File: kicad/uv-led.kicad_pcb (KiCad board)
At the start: 2 copper layers, 100 x 8 mm, 10 parts, among them J1 JST_PH_B2B-PH-K_1x02_P2.00mm_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

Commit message: updated physical stackup and removed back paste
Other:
- board text added: "Manufacturing Instruction: - Material Aluminum - Finished thickness: 1.6 mm ± 0.16 mm - PCBs must be RoHS compliant - Do not edit artwork, e.g. to add logos or order numbers - Clean to meet IPC J-STD-001E, Class 2 after assembly"
- board text removed: "Manufacturing Instruction: - Material Aluminum - Finished thickness: 1.57 mm ± 0.13 mm - PCBs must be RoHS compliant - Do not edit artwork, e.g. to add logos or order numbers - Clean to meet IPC J-STD-001E, Class 2 after assembly"

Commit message: Fixed BOM (#18)
- Fixed JST PN
- Fixed LED temperature
- Bumped to v1.1.1
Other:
- board text added: "UV-LED Design: T. Guentzel Date: 2026-09 Version: 1.1.1"
- board text removed: "UV-LED Design: T. Guentzel Date: 2026-09 Version: 1.1.0"
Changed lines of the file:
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@@
 		(title "QUIPS-C UV-LED")
 		(date "2026-09-02")
-		(rev "1.1.0")
+		(rev "1.1.1")
 		(company "TU Darmstadt")
 		(comment 1 "Copyright (©) 2026, Tom Güntzel <tom.guentzel@physik.tu-darmstadt.de>")
@@
 		(capping no)
 		(filling no)
-		(zone_defaults)
 		(pcbplotparams
 			(layerselection 0x00000000_00000000_55555555_5755f5ff)
@@
 		(sheetname "/")
 		(sheetfile "uv-led.kicad_sch")
+		(units
+			(unit
+				(name "A")
+				(pins)
+			)
+		)
 		(attr exclude_from_bom)
 		(duplicate_pad_numbers_are_jumpers no)
@@
 				(font
 					(size 1.27 1.27)
-				)
-			)
-		)
-		(property "KiLib_Generator" "mounting_hardware/mounting_hole"
-			(at 0 0 0)
-			(layer "F.SilkS")
-			(hide yes)
-			(effects
-				(font
-					(size 1 1)
-					(thickness 0.15)
 				)
 			)
@@
 			)
 		)
-		(property "MN" ""
-			(at 0 0 0)
-			(unlocked yes)
-			(layer "F.Fab")
-			(hide yes)
-			(effects
-				(font
-					(size 1 1)
-					(thickness 0.15)
-				)
-			)
-		)
-		(property "Mfr" ""
-			(at 0 0 0)
-			(unlocked yes)
-			(layer "F.Fab")
-			(hide yes)
-			(effects
-				(font
-					(size 1 1)
-					(thickness 0.15)
-				)
-			)
-		)
-		(property "Temperature" "Top = 0 °C to 100 °C"
+		(property "Temperature" "Top = -40 °C to 95 °C"
 			(at 0 0 0)
 			(unlocked yes)
@@
 			)
 		)
-		(property "MN" ""
-			(at 0 0 0)
-			(unlocked yes)
-			(layer "F.Fab")
-			(hide yes)
-			(effects
-				(font
-					(size 1 1)
-					(thickness 0.15)
-				)
-			)
-		)
-		(property "Mfr" ""
-			(at 0 0 0)
-			(unlocked yes)
-			(layer "F.Fab")
-			(hide yes)
-			(effects
-				(font
-					(size 1 1)
-					(thickness 0.15)
-				)
-			)
-		)
-		(property "Temperature" "Top = 0 °C to 100 °C"
+		(property "Temperature" "Top = -40 °C to 95 °C"
 			(at 0 0 0)
 			(unlocked yes)
@@
 			)
 		)
-		(property "MN" ""
-			(at 0 0 0)
-			(unlocked yes)
-			(layer "F.Fab")
-			(hide yes)
-			(effects
-				(font
-					(size 1 1)
-					(thickness 0.15)
-				)
-			)
-		)
-		(property "Mfr" ""
-			(at 0 0 0)
-			(unlocked yes)
-			(layer "F.Fab")
-			(hide yes)
-			(effects
-				(font
-					(size 1 1)
-					(thickness 0.15)
-				)
-			)
-		)
-		(property "Temperature" "Top = 0 °C to 100 °C"
+		(property "Temperature" "Top = -40 °C to 95 °C"
 			(at 0 0 0)
 			(unlocked yes)
@@
 			)
 		)
-		(property "MN" ""
-			(at 0 0 0)
-			(unlocked yes)
-			(layer "F.Fab")
-			(hide yes)
-			(effects
-				(font
-					(size 1 1)
-					(thickness 0.15)
-				)
-			)
-		)
-		(property "Mfr" ""
-			(at 0 0 0)
-			(unlocked yes)
-			(layer "F.Fab")
-			(hide yes)
-			(effects
-				(font
-					(size 1 1)
-					(thickness 0.15)
-				)
-			)
-		)
-		(property "Temperature" "Top = 0 °C to 100 °C"
+		(property "Temperature" "Top = -40 °C to 95 °C"
 			(at 0 0 0)
 			(unlocked yes)
@@
 			)
 		)
-		(property "MN" ""
-			(at 0 0 0)
-			(unlocked yes)
-			(layer "F.Fab")
-			(hide yes)
-			(effects
-				(font
-					(size 1 1)
-					(thickness 0.15)
-				)
-			)
-		)
-		(property "Mfr" ""
-			(at 0 0 0)
-			(unlocked yes)
-			(layer "F.Fab")
-			(hide yes)
-			(effects
-				(font
-					(size 1 1)
-					(thickness 0.15)
-				)
-			)
-		)
-		(property "Temperature" "Top = 0 °C to 100 °C"
+		(property "Temperature" "Top = -40 °C to 95 °C"
 			(at 0 0 0)
 			(unlocked yes)
@@
 				(font
 					(size 1.27 1.27)
-				)
-			)
-		)
-		(property "KiLib_Generator" "mounting_hardware/mounting_hole"
-			(at 0 0 0)
-			(layer "F.SilkS")
-			(hide yes)
-			(effects
-				(font
-					(size 1 1)
-					(thickness 0.15)
 				)
 			)
@@
 			)
 		)
-		(property "KiLib_Generator" "SMD_2terminal_chip_molded"
-			(at 0 0 0)
-			(layer "F.SilkS")
-			(hide yes)
-			(effects
-				(font
-					(size 1 1)
-					(thickness 0.15)
-				)
-			)
-		)
 		(property "PN" "CRCW12184R02FKEKHP"
 			(at 0 0 0)
@@
 			)
 		)
-		(property "KiLib_Generator" "connector/JST"
-			(at 0 0 0)
-			(layer "B.SilkS")
+		(property "MFN" "JST Commercial"
+			(at 0 0 0)
+			(unlocked yes)
+			(layer "B.Fab")
 			(hide yes)
 			(effects
@@
 			)
 		)
-		(property "MN" ""
-			(at 0 0 180)
+		(property "PN" "B2B-PH-K(LF)(SN)"
+			(at 0 0 0)
 			(unlocked yes)
 			(layer "B.Fab")
@@
 			)
 		)
-		(property "Mfr" ""
-			(at 0 0 180)
+		(property "RoHS" "Yes"
+			(at 0 0 0)
 			(unlocked yes)
 			(layer "B.Fab")
@@
 			)
 		)
-		(property "MFN" "JST Commercial"
+		(property "Temperature" "Top = -25 °C to 85 °C"
 			(at 0 0 0)
 			(unlocked yes)
@@
 			)
 		)
-		(property "PN" "PH_B2B-PH-K_1x02_P2.00mm_Vertical"
-			(at 0 0 0)
-			(unlocked yes)
-			(layer "B.Fab")
-			(hide yes)
-			(effects
-				(font
-					(size 1 1)
-					(thickness 0.15)
-				)
-				(justify mirror)
-			)
-		)
-		(property "RoHS" "By exemption"
-			(at 0 0 0)
-			(unlocked yes)
-			(layer "B.Fab")
-			(hide yes)
-			(effects
-				(font
-					(size 1 1)
-					(thickness 0.15)
-				)
-				(justify mirror)
-			)
-		)
-		(property "Temperature" "Top = -25 °C to 85 °C"
+		(property "Alternative" "JST B2B-PH-KL(LF)(SN)"
 			(at 0 0 0)
 			(unlocked yes)
@@
 		(layer "Edge.Cuts")
 	)
-	(gr_text "UV-LED\nDesign: T. Guentzel\nDate: 2026-09\nVersion: 1.1.0"
+	(gr_text "UV-LED\nDesign: T. Guentzel\nDate: 2026-09\nVersion: 1.1.1"
 		(at 123.25 102.42 0)
 		(layer "F.SilkS")

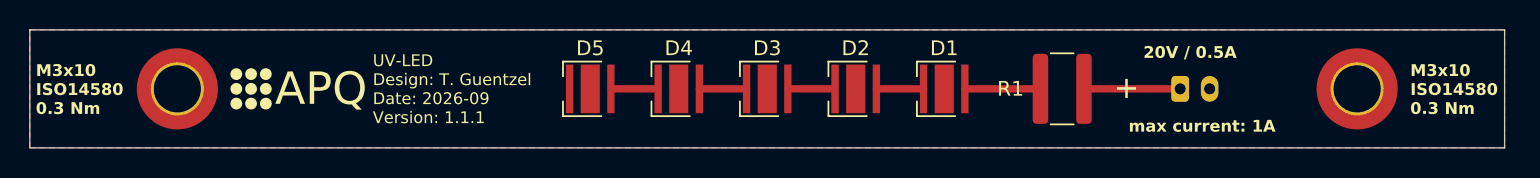
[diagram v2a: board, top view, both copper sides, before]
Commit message: Feature/two layer PCB with vias (#19)
* enlarged drill holes for M6 screws for more tolerance

* updated mount revision number to 1.2.0

* updated revision number to 1.2.0

* updated PCB revision label

* screw pads changed to unconnected

* updated physical stackup to two 70um copper layers

* Added missing infos

- Missing dimension
- Moved J1 label
- Added board finish

---------

Co-authored-by: Patrick Baus <patrick.baus@physik.tu-darmstadt.de>
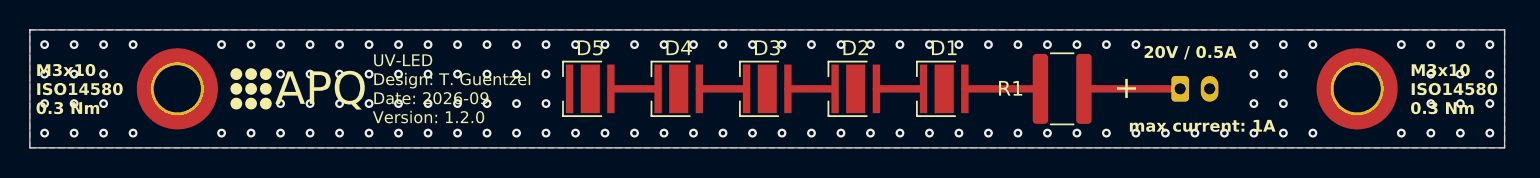
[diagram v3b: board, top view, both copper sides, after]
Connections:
- H1 pad 1: GND -> unconnected-(H1-Pad1)_1
- H2 pad 1: GND -> unconnected-(H2-Pad1)
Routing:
- net GND: vias 0 -> 127
- added copper zone on B.Cu, net GND
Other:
- board text added: "Manufacturing Instruction: - Material FR4 - Finished thickness: 1.6 mm ± 0.16 mm - PCBs must be RoHS compliant - Do not edit artwork, e.g. to add logos or order numbers - Clean to meet IPC J-STD-001E, Class 2 after assembly"
- board text added: "UV-LED Design: T. Guentzel Date: 2026-09 Version: 1.2.0"
- board text removed: "Manufacturing Instruction: - Material Aluminum - Finished thickness: 1.6 mm ± 0.16 mm - PCBs must be RoHS compliant - Do not edit artwork, e.g. to add logos or order numbers - Clean to meet IPC J-STD-001E, Class 2 after assembly"
- board text removed: "UV-LED Design: T. Guentzel Date: 2026-09 Version: 1.1.1"
